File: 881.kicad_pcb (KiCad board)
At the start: 2 copper layers, 38 x 105 mm, 79 parts, among them J1 BD TRIG, J10 CY TRIG, J11 OH TRIG, J12 CH_TRIG, J13 ACCENT IN, J14 RUN/STOP, J15 RESET, J16 CLOCK OUT, J17 ACCENT OUT, J2 SD TRIG, J3 LT TRIG, J4 MT TRIG, J5 HT_TRIG, J6 RS TRIG, J7 CP_TRIG, J8 MA_TRIG, J9 CB TRIG, P1 CONN_02X03, P2 CONN_02X10, SW1 SPDT, U1 CD4048B, U2 CD4048B, X1 SYNC24 OUT, X2 MIDI OUT

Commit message: placed and routed
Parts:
- SW1: footprint MyModules:SS-12F45-1P2T-SLIDE -> MyModules:SS-12F108-1P2T-SLIDE
- moved C3 75.1 mm to (142.8, 71.0), turned to 0 degrees
- moved U2 74.9 mm to (143.5, 74.8)
- moved U1 74.7 mm to (116.8, 74.8)
- moved C2 73.7 mm to (114.8, 71.0), turned to 180 degrees
- moved R16 61.7 mm to (114.5, 149.2), turned to 90 degrees
- moved D25 59.8 mm to (120.2, 149.2), turned to 90 degrees
- moved D26 59.4 mm to (121.8, 149.2), turned to 270 degrees
- moved R20 58.0 mm to (146.5, 149.2), turned to 90 degrees
- moved D20 49.4 mm to (120.2, 138.2), turned to 90 degrees
- moved D19 48.9 mm to (121.8, 138.2), turned to 270 degrees
- moved D21 48.3 mm to (123.8, 138.2), turned to 270 degrees
- moved D24 46.3 mm to (136.2, 138.2), turned to 90 degrees
- moved R12 46.1 mm to (120.2, 134.8), turned to 90 degrees
- moved D22 45.5 mm to (125.2, 135.8), turned to 270 degrees
- moved R13 45.3 mm to (126.8, 136.0), turned to 90 degrees
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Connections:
- U1 pad 11: /RS_TRIG -> /BD_TRIG
- U1 pad 12: /CP_TRIG -> /SD_TRIG
- U1 pad 13: /SD_TRIG -> /CP_TRIG
- U1 pad 14: /BD_TRIG -> /RS_TRIG
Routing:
- net +5V: track 0.00 -> 218.0 mm, vias 0 -> 12
- net Net-(SW1-Pad2): track 0.00 -> 90.9 mm, vias 0 -> 1
- net /CY_TRIG: track 0.00 -> 87.8 mm, vias 0 -> 1
- net /OH_TRIG: track 0.00 -> 86.1 mm, vias 0 -> 1
- net GND: track 0.00 -> 76.8 mm, vias 0 -> 9
- net COMMON_TRIG: track 0.00 -> 75.4 mm, vias 0 -> 1
- net /CH_TRIG: track 0.00 -> 75.2 mm, vias 0 -> 3
- net /CP_TRIG: track 0.00 -> 69.3 mm, vias 0 -> 2
- net /CB_TRIG: track 0.00 -> 68.2 mm
- net /TRIG: track 0.00 -> 65.2 mm
- net /MA_TRIG: track 0.00 -> 59.3 mm, vias 0 -> 1
- net /MT_TRIG: track 0.00 -> 59.1 mm, vias 0 -> 2
- net /ACCENT: track 0.00 -> 58.8 mm, vias 0 -> 1
- net /RS_TRIG: track 0.00 -> 55.3 mm
- net /LT_TRIG: track 0.00 -> 47.2 mm, vias 0 -> 1
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- added copper zone on B.Cu, net GND
- added copper zone on F.Cu, net GND
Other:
- net class Default: via_dia 0.6 -> 0.8
- net class POWER added: clearance 0.25, trace_width 0.35, via_dia 0.9, via_drill 0.45

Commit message: ground stitching, tweaking
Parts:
- moved R17 0.60 mm to (121.3, 79.4)
- moved D27 0.35 mm to (121.5, 80.9)
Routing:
- net GND: track 76.8 -> 91.6 mm, vias 9 -> 13
- net Net-(D27-Pad2): track 5.50 -> 7.55 mm
- net /HT_TRIG: track 46.9 -> 48.0 mm
- net /CY_TRIG: track 87.8 -> 88.8 mm
- net +5V: track 218.0 -> 217.0 mm
- net UART_TX: track 15.4 -> 16.3 mm
- net /CH_TRIG: track 75.2 -> 76.0 mm
- net /CB_TRIG: track 68.2 -> 68.9 mm
- net /LT_TRIG: track 47.2 -> 47.9 mm
- net /MT_TRIG: track 59.1 -> 59.7 mm

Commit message: first prototype PCB ordered
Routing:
- net +5V: track 217.0 -> 217.6 mm
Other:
- rule pad_to_mask_clearance: 0.2 -> 0.025
- board text added: "881"
- board text added: "CLOCK OUT"
- board text added: "MIDI OUT"
- board text added: "RESET"
- board text added: "RUN/STOP"
- board text added: "SYNC24"
- board text added: "TRIGGER EXPANDER"
- board text added: "r1.0 10/2018"
- board text added: "system80.net"

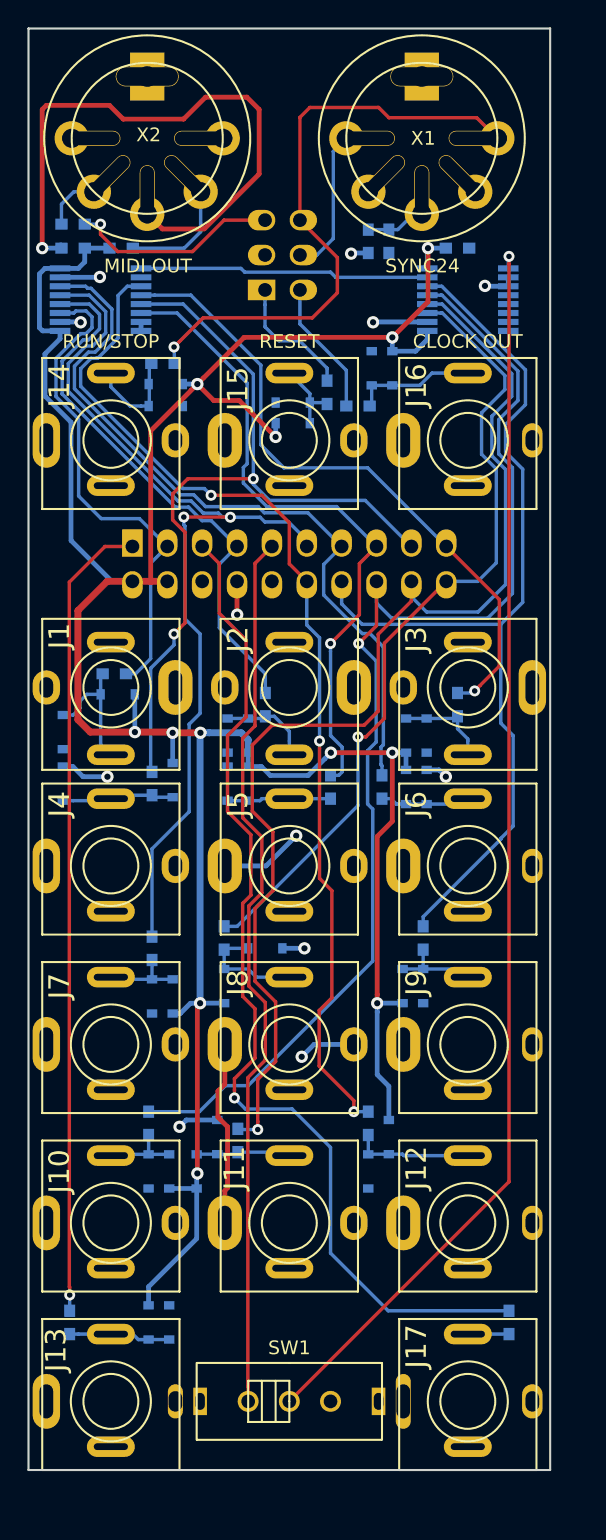
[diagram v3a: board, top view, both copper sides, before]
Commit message: schematic and footprint almost complete. spi clock or run-stop line for TII active indication still debatable, but leaning towards SPI SCK for LED indication
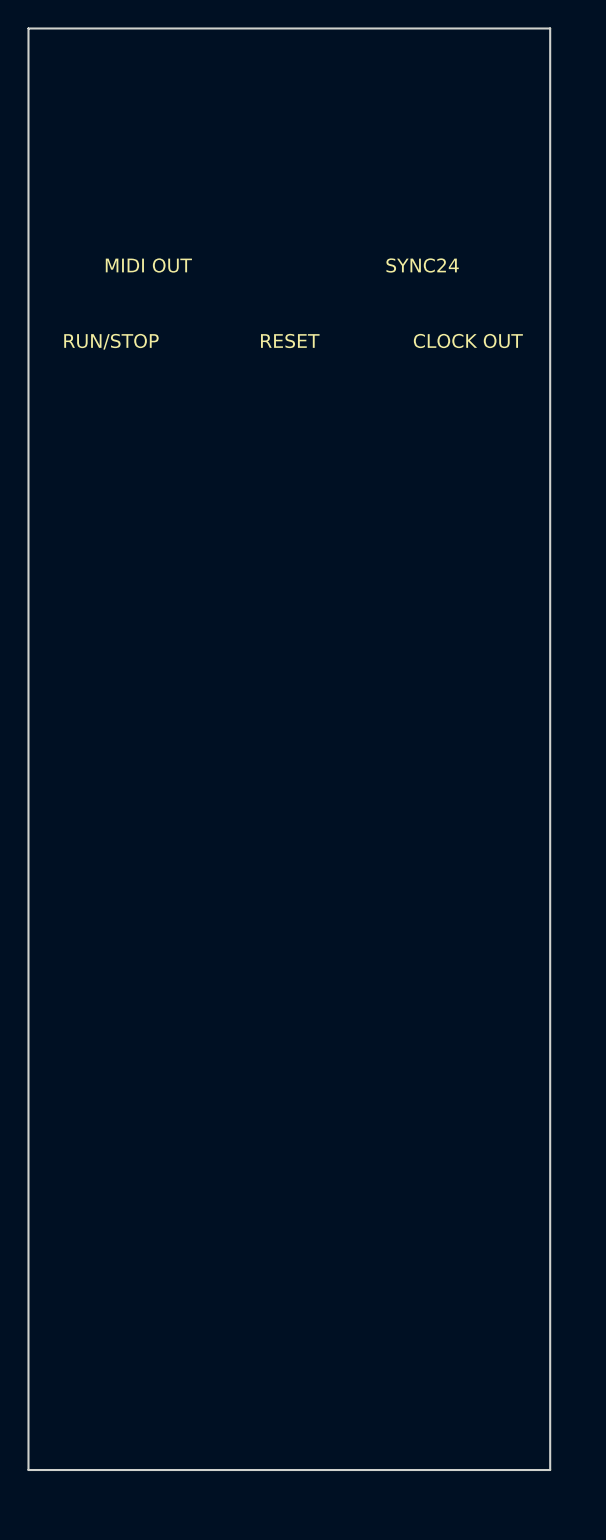
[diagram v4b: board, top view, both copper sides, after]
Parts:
- removed C1: 0.01µ, MyModules:SM0603-C-MURATA
- removed C2, C3: 0.1µ, MyModules:SM0603-C-MURATA
- removed D1, D10, D11, D12, D13, D14, D15, D16, D17, D18, D19, D2, D20, D21, D22, D23, D24, D25, D26, D27, D28, D29, D3, D30, D31, D32, D4, D5, D6, D7, D8, D9: NSR0530HT1G, MyModules:SOD323-C1A2
- removed J1: BD TRIG, MyModules:PJ-301B-JACK-SLOTS
- removed J10: CY TRIG, MyModules:PJ-301B-JACK-SLOTS
- removed J11: OH TRIG, MyModules:PJ-301B-JACK-SLOTS
- removed J12: CH_TRIG, MyModules:PJ-301B-JACK-SLOTS
- removed J13: ACCENT IN, MyModules:PJ-301B-JACK-SLOTS
- removed J14: RUN/STOP, MyModules:PJ-301B-JACK-SLOTS
- removed J15: RESET, MyModules:PJ-301B-JACK-SLOTS
- removed J16: CLOCK OUT, MyModules:PJ-301B-JACK-SLOTS
- removed J17: ACCENT OUT, MyModules:PJ-301B-JACK-SLOTS
- removed J2: SD TRIG, MyModules:PJ-301B-JACK-SLOTS
- removed J3: LT TRIG, MyModules:PJ-301B-JACK-SLOTS
- removed J4: MT TRIG, MyModules:PJ-301B-JACK-SLOTS
- removed J5: HT_TRIG, MyModules:PJ-301B-JACK-SLOTS
- removed J6: RS TRIG, MyModules:PJ-301B-JACK-SLOTS
- removed J7: CP_TRIG, MyModules:PJ-301B-JACK-SLOTS
- removed J8: MA_TRIG, MyModules:PJ-301B-JACK-SLOTS
- removed J9: CB TRIG, MyModules:PJ-301B-JACK-SLOTS
- removed P1: CONN_02X03, w_conn_strip:vasch_strip_3x2
- removed P2: CONN_02X10, w_conn_strip:vasch_strip_10x2
- removed R1, R10, R11, R12, R13, R14, R15, R16, R17, R18, R19, R2, R20, R3, R4, R6, R7, R8, R9: 220, MyModules:SM0603-R-YAGEO
- removed R5: 22, MyModules:SM0603-R-YAGEO
- removed SW1: SPDT, MyModules:SS-12F108-1P2T-SLIDE
- removed U1, U2: CD4048B, Housings_SSOP:TSSOP-16_4.4x5mm_Pitch0.65mm
- removed X1: SYNC24 OUT, MyModules:SD-50BV-5DIN-SLOTS
- removed X2: MIDI OUT, MyModules:SD-50BV-5DIN-SLOTS
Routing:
- net +5V: track 217.6 -> 0.00 mm, vias 12 -> 0
- net GND: track 91.6 -> 0.00 mm, vias 13 -> 0
- net Net-(SW1-Pad2): track 90.9 -> 0.00 mm, vias 1 -> 0
- net /CY_TRIG: track 88.8 -> 0.00 mm, vias 1 -> 0
- net /OH_TRIG: track 86.3 -> 0.00 mm, vias 1 -> 0
- net /CH_TRIG: track 76.0 -> 0.00 mm, vias 3 -> 0
- net COMMON_TRIG: track 75.4 -> 0.00 mm, vias 1 -> 0
- net /CP_TRIG: track 69.3 -> 0.00 mm, vias 2 -> 0
- net /CB_TRIG: track 68.9 -> 0.00 mm
- net /TRIG: track 65.2 -> 0.00 mm
- net /MT_TRIG: track 59.8 -> 0.00 mm, vias 2 -> 0
- net /MA_TRIG: track 59.3 -> 0.00 mm, vias 1 -> 0
- net /ACCENT: track 58.8 -> 0.00 mm, vias 1 -> 0
- net /RS_TRIG: track 55.3 -> 0.00 mm
- net /HT_TRIG: track 48.0 -> 0.00 mm, vias 1 -> 0
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- removed copper zone on B.Cu, net GND
- removed copper zone on F.Cu, net GND
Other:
- board text added: "r2.0 10/2020"
- board text removed: "881"
- board text removed: "r1.0 10/2018"

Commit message: first route
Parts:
- added C1: 0.01µ, MyModules:SM0603-C-MURATA, B.Cu at (121.5, 91.8)
- added C15: 1µ, Capacitors_SMD:C_0805, B.Cu at (129.5, 79.0)
- added C19: 0.1µ, MyModules:SM0603-C-MURATA, B.Cu at (129.2, 77.2)
- added C2: 0.1µ, MyModules:SM0603-C-MURATA, B.Cu at (115.0, 76.5)
- added C20: 0.1µ, MyModules:SM0603-C-MURATA, B.Cu at (143.5, 76.8)
- added C3: 0.1µ, MyModules:SM0603-C-MURATA, B.Cu at (137.0, 76.5)
- added C4: 1n, MyModules:SM0603-C-MURATA, B.Cu at (134.2, 152.2)
- added D1: B5819W, Diodes_SMD:D_SOD-123, B.Cu at (115.8, 153.5)
- added D10: 1N4148, Diodes_SMD:D_SOD-323F, B.Cu at (141.8, 114.0)
- added D11: 1N4148, Diodes_SMD:D_SOD-323F, B.Cu at (115.8, 127.0)
- added D12: 1N4148, Diodes_SMD:D_SOD-323F, B.Cu at (128.8, 127.0)
- added D13: 1N4148, Diodes_SMD:D_SOD-323F, B.Cu at (141.8, 127.0)
- added D14: 1N4148, Diodes_SMD:D_SOD-323F, B.Cu at (115.8, 140.0)
- added D15: 1N4148, Diodes_SMD:D_SOD-323F, B.Cu at (128.8, 140.0)
- added D16: 1N4148, Diodes_SMD:D_SOD-323F, B.Cu at (141.8, 139.8)
- added D17: LED, LEDs:LED_0805, B.Cu at (130.5, 155.0)
- added D18: LED, LEDs:LED_D3.0mm, F.Cu at (130.5, 153.8)
- added D2: B5819W, Diodes_SMD:D_SOD-123, B.Cu at (119.5, 153.5)
- added D3: B5819W, Diodes_SMD:D_SOD-123, B.Cu at (141.8, 153.8)
- added D4: B5819W, Diodes_SMD:D_SOD-123, B.Cu at (145.5, 153.8)
- added D5: 1N4148, Diodes_SMD:D_SOD-323F, B.Cu at (116.0, 101.0)
- added D6: 1N4148, Diodes_SMD:D_SOD-323F, B.Cu at (129.0, 101.0)
- added D7: 1N4148, Diodes_SMD:D_SOD-323F, B.Cu at (141.9, 101.0)
- added D8: 1N4148, Diodes_SMD:D_SOD-323F, B.Cu at (115.8, 114.0)
- added D9: 1N4148, Diodes_SMD:D_SOD-323F, B.Cu at (128.8, 114.0)
- added ISP1: CONN_02X03, w_conn_strip:vasch_strip_3x2, B.Cu at (130.5, 88.5)
- added J1: RUN/STOP, MyModules:PJ-301B-JACK-SLOTS, F.Cu at (120.0, 61.0)
- added J10: RS IN, MyModules:PJ-301B-JACK-SLOTS, F.Cu at (143.5, 116.0)
- added J11: CP IN, MyModules:PJ-301B-JACK-SLOTS, F.Cu at (117.5, 129.0)
- added J12: MA IN, MyModules:PJ-301B-JACK-SLOTS, F.Cu at (130.5, 129.0)
- added J13: CB IN, MyModules:PJ-301B-JACK-SLOTS, F.Cu at (143.5, 129.0)
- added J14: CY IN, MyModules:PJ-301B-JACK-SLOTS, F.Cu at (117.5, 142.0)
- added J15: OH IN, MyModules:PJ-301B-JACK-SLOTS, F.Cu at (130.5, 142.0)
- added J16: CH IN, MyModules:PJ-301B-JACK-SLOTS, F.Cu at (143.5, 142.0)
- added J2: SYNC24 CLK, MyModules:PJ-301B-JACK-SLOTS, F.Cu at (141.0, 61.0)
- added J3: ASSIGN 1, MyModules:PJ-301B-JACK-SLOTS, F.Cu at (117.5, 155.0)
- added J4: ASSIGN 2, MyModules:PJ-301B-JACK-SLOTS, F.Cu at (143.5, 155.0)
- added J5: BD IN, MyModules:PJ-301B-JACK-SLOTS, F.Cu at (117.5, 103.0)
- added J6: SD IN, MyModules:PJ-301B-JACK-SLOTS, F.Cu at (130.5, 103.0)
- added J7: LT IN, MyModules:PJ-301B-JACK-SLOTS, F.Cu at (143.5, 103.0)
- added J8: MT IN, MyModules:PJ-301B-JACK-SLOTS, F.Cu at (117.5, 116.0)
- added J9: HT IN, MyModules:PJ-301B-JACK-SLOTS, F.Cu at (130.5, 116.0)
- added P1: CONN_02X03, w_conn_strip:vasch_strip_4x2, B.Cu at (130.5, 64.5)
- added Q1: MMBT3904, MyModules:SOT23-132-JRL, B.Cu at (121.2, 98.8)
- added Q10: MMBT3904, MyModules:SOT23-132-JRL, B.Cu at (121.2, 137.8)
- added Q11: MMBT3904, MyModules:SOT23-132-JRL, B.Cu at (134.2, 137.8)
- added Q12: MMBT3904, MyModules:SOT23-132-JRL, B.Cu at (147.2, 137.8)
- added Q13: MMBT3904, MyModules:SOT23-132-JRL, B.Cu at (135.0, 147.8)
- added Q14: MMBT3906, SOT-23, B.Cu at (130.5, 150.5)
- added Q2: MMBT3904, MyModules:SOT23-132-JRL, B.Cu at (134.2, 98.8)
- added Q3: MMBT3904, MyModules:SOT23-132-JRL, B.Cu at (147.5, 98.8)
- added Q4: MMBT3904, MyModules:SOT23-132-JRL, B.Cu at (121.2, 111.8)
- added Q5: MMBT3904, MyModules:SOT23-132-JRL, B.Cu at (134.2, 111.8)
- added Q6: MMBT3904, MyModules:SOT23-132-JRL, B.Cu at (147.2, 111.8)
- added Q7: MMBT3904, MyModules:SOT23-132-JRL, B.Cu at (121.2, 124.8)
- added Q8: MMBT3904, MyModules:SOT23-132-JRL, B.Cu at (134.2, 124.8)
- added Q9: MMBT3904, MyModules:SOT23-132-JRL, B.Cu at (147.2, 124.8)
- added R1: 220, MyModules:SM0603-R-YAGEO, B.Cu at (138.2, 83.0)
- added R10: 100K, MyModules:SM0603-R-YAGEO, B.Cu at (119.0, 101.0)
- added R11: 100K, MyModules:SM0603-R-YAGEO, B.Cu at (132.0, 101.0)
- added R12: 100K, MyModules:SM0603-R-YAGEO, B.Cu at (145.2, 101.0)
- added R13: 100K, MyModules:SM0603-R-YAGEO, B.Cu at (119.0, 114.0)
- added R14: 10K, MyModules:SM0603-R-YAGEO, B.Cu at (120.2, 96.0)
- added R15: 10K, MyModules:SM0603-R-YAGEO, B.Cu at (136.2, 96.2)
- added R16: 10K, MyModules:SM0603-R-YAGEO, B.Cu at (146.5, 96.0)
- added R17: 10K, MyModules:SM0603-R-YAGEO, B.Cu at (120.2, 109.0)
- added R18: 100K, MyModules:SM0603-R-YAGEO, B.Cu at (130.5, 114.0)
- added R19: 100K, MyModules:SM0603-R-YAGEO, B.Cu at (143.5, 114.0)
- added R2: 22, MyModules:SM0603-R-YAGEO, B.Cu at (120.0, 91.8)
- added R20: 100K, MyModules:SM0603-R-YAGEO, B.Cu at (117.5, 127.0)
- added R21: 100K, MyModules:SM0603-R-YAGEO, B.Cu at (130.5, 127.0)
- added R22: 100K, MyModules:SM0603-R-YAGEO, B.Cu at (132.0, 114.0)
- added R23: 100K, MyModules:SM0603-R-YAGEO, B.Cu at (145.0, 114.0)
- added R24: 100K, MyModules:SM0603-R-YAGEO, B.Cu at (119.0, 127.0)
- added R25: 100K, MyModules:SM0603-R-YAGEO, B.Cu at (132.0, 127.0)
- added R26: 10K, MyModules:SM0603-R-YAGEO, B.Cu at (133.2, 109.0)
- added R27: 10K, MyModules:SM0603-R-YAGEO, B.Cu at (146.2, 109.0)
- added R28: 10K, MyModules:SM0603-R-YAGEO, B.Cu at (120.2, 122.0)
- added R29: 10K, MyModules:SM0603-R-YAGEO, B.Cu at (133.2, 122.0)
- added R3: 220, MyModules:SM0603-R-YAGEO, B.Cu at (143.8, 83.0)
- added R30: 100K, MyModules:SM0603-R-YAGEO, B.Cu at (143.5, 127.0)
- added R31: 100K, MyModules:SM0603-R-YAGEO, B.Cu at (117.5, 140.0)
- added R32: 100K, MyModules:SM0603-R-YAGEO, B.Cu at (130.5, 140.0)
- added R33: 100K, MyModules:SM0603-R-YAGEO, B.Cu at (143.5, 140.0)
- added R34: 100K, MyModules:SM0603-R-YAGEO, B.Cu at (145.0, 127.0)
- added R35: 100K, MyModules:SM0603-R-YAGEO, B.Cu at (119.0, 140.0)
- added R36: 100K, MyModules:SM0603-R-YAGEO, B.Cu at (132.0, 140.0)
- added R37: 100K, MyModules:SM0603-R-YAGEO, B.Cu at (145.0, 140.0)
- added R38: 10K, MyModules:SM0603-R-YAGEO, B.Cu at (146.2, 122.0)
- added R39: 10K, MyModules:SM0603-R-YAGEO, B.Cu at (120.2, 135.0)
- added R4: 1K, MyModules:SM0603-R-YAGEO, B.Cu at (121.2, 149.5)
- added R40: 10K, MyModules:SM0603-R-YAGEO, B.Cu at (133.2, 135.0)
- added R41: 10K, MyModules:SM0603-R-YAGEO, B.Cu at (146.0, 135.0)
- added R42: 47K, MyModules:SM0603-R-YAGEO, B.Cu at (122.2, 151.8)
- added R43: 100K, MyModules:SM0603-R-YAGEO, B.Cu at (148.2, 151.8)
- added R44: 47K, MyModules:SM0603-R-YAGEO, B.Cu at (147.0, 80.0)
- added R45: 47K, MyModules:SM0603-R-YAGEO, B.Cu at (148.5, 80.0)
- added R46: 100K, MyModules:SM0603-R-YAGEO, B.Cu at (135.0, 145.0)
- added R47: 1K, MyModules:SM0603-R-YAGEO, B.Cu at (137.0, 150.2)
- added R48: 10K, MyModules:SM0603-R-YAGEO, B.Cu at (134.2, 150.8)
- added R49: 1K, MyModules:SM0603-R-YAGEO, B.Cu at (134.5, 155.0)
- added R5: 1K, MyModules:SM0603-R-YAGEO, B.Cu at (147.2, 149.5)
- added R6: 100K, MyModules:SM0603-R-YAGEO, B.Cu at (117.5, 101.0)
- added R7: 100K, MyModules:SM0603-R-YAGEO, B.Cu at (130.5, 101.0)
- added R8: 100K, MyModules:SM0603-R-YAGEO, B.Cu at (143.8, 101.0)
- added R9: 100K, MyModules:SM0603-R-YAGEO, B.Cu at (117.5, 114.0)
- added TP2: CONN_1, MyModules:TEST_POINT_LOOP_4592, B.Cu at (126.5, 56.5)
- added U1: 74HC165, Housings_SOIC:SOIC-16_3.9x9.9mm_Pitch1.27mm, B.Cu at (119.5, 71.0)
- added U2: 74HC165, Housings_SOIC:SOIC-16_3.9x9.9mm_Pitch1.27mm, B.Cu at (141.5, 71.0)
- added U7: 74AHCT1G125GW, TO_SOT_Packages_SMD:SOT-353_SC-70-5, B.Cu at (146.2, 76.8)
- added X1: MIDI OUT, MyModules:SD-50BV-5DIN, F.Cu at (141.0, 83.0)
- added X2: SYNC24, MyModules:SD-50BV-5DIN, F.Cu at (120.0, 83.0)
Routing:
- net DIN_RESET: track 0.00 -> 143.3 mm, vias 0 -> 1
- net ISP_SCK: track 0.00 -> 117.2 mm, vias 0 -> 3
- net DIN_FILL: track 0.00 -> 109.5 mm, vias 0 -> 1
- net /HT: track 0.00 -> 85.3 mm
- net /CY: track 0.00 -> 77.1 mm, vias 0 -> 2
- net /RS: track 0.00 -> 75.7 mm, vias 0 -> 2
- net /CH: track 0.00 -> 72.6 mm, vias 0 -> 2
- net /OH: track 0.00 -> 67.1 mm, vias 0 -> 2
- net DIN_RUN_STOP: track 0.00 -> 67.0 mm, vias 0 -> 1
- net /MA: track 0.00 -> 60.5 mm, vias 0 -> 2
- net /CP: track 0.00 -> 56.4 mm, vias 0 -> 2
- net /CB: track 0.00 -> 54.5 mm, vias 0 -> 2
- net DIN_TEMPO_CLK: track 0.00 -> 53.4 mm
- net /LT: track 0.00 -> 52.5 mm
- net ISP_MOSI: track 0.00 -> 47.2 mm, vias 0 -> 2
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- added copper zone on In2.Cu, net +5V
- added copper zone on B.Cu, net GNDD
- added copper zone on F.Cu, net GNDD
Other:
- copper layers 2 -> 4
- net class Default: via_dia 0.8 -> 0.9; via_drill 0.4 -> 0.45
- net class POWER: via_dia 0.9 -> 1; via_drill 0.45 -> 0.5

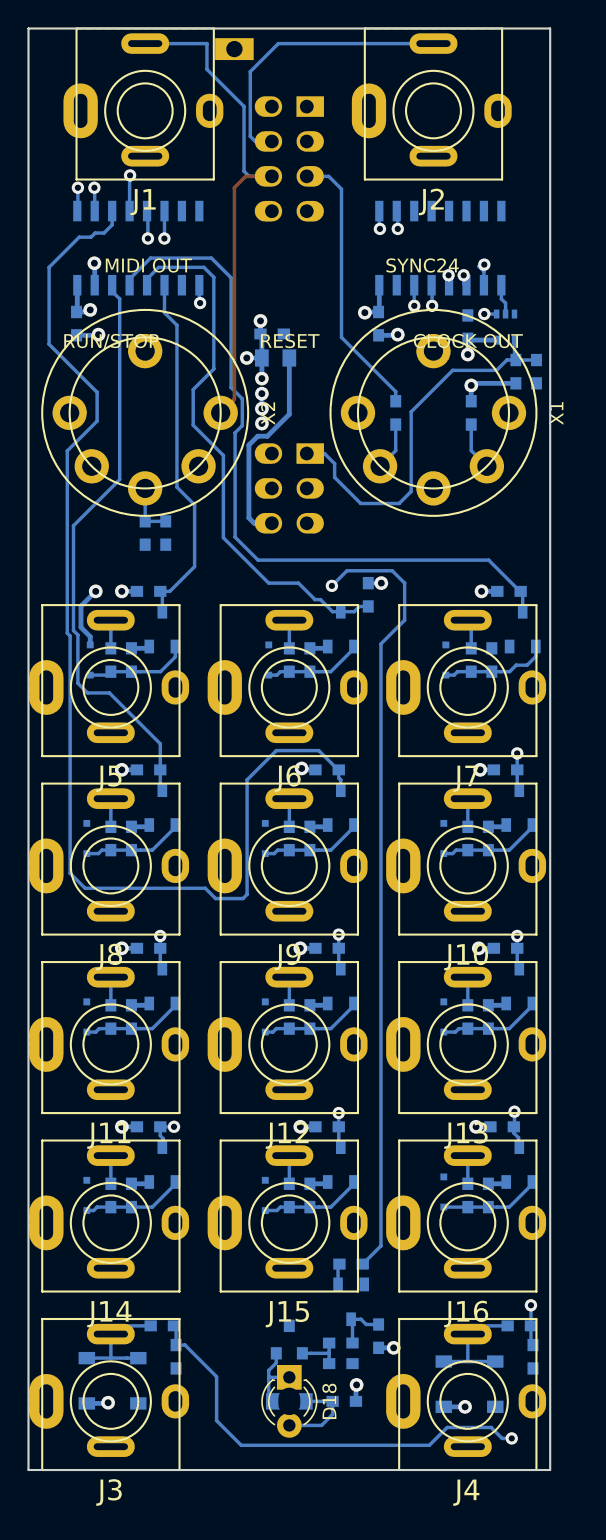
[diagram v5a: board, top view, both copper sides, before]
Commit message: routed with more finesse
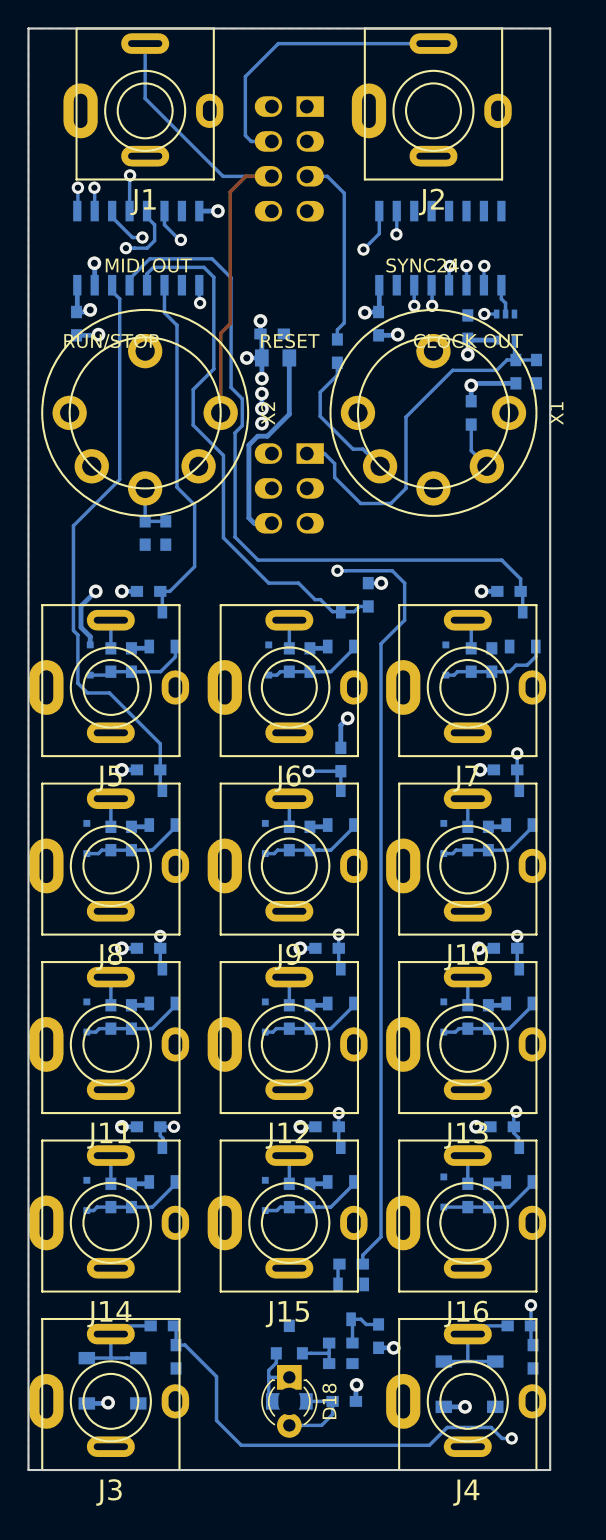
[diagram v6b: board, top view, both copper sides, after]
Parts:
- removed TP2: CONN_1, MyModules:TEST_POINT_LOOP_4592
- moved R1 6.19 mm to (134.0, 78.5)
- moved R26 1.25 mm to (134.2, 108.2), turned to 270 degrees
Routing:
- net /HT: track 85.3 -> 52.0 mm, vias 0 -> 2
- net Net-(R1-Pad1): track 3.51 -> 10.3 mm
- net UART_TX: track 20.0 -> 14.1 mm
- net ISP_SCK: track 117.2 -> 112.5 mm
- net /CP: track 56.4 -> 58.6 mm
- net /CY: track 77.1 -> 79.2 mm
- net DIN_RESET: track 143.3 -> 144.9 mm
- net DIN_RUN_STOP: track 67.0 -> 65.5 mm
- net GNDD: track 39.3 -> 40.6 mm, vias 4 -> 5
- net +5V: track 40.7 -> 42.0 mm
- net ISP_MOSI: track 47.2 -> 48.4 mm
- net /CB: track 54.5 -> 55.6 mm
- net DIN_FILL: track 109.5 -> 110.4 mm
- net /MA: track 60.5 -> 61.2 mm

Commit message: routed, finessed, ready to order me thinks
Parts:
- removed R45: 47K, MyModules:SM0603-R-YAGEO
- added SNAP-HOLE-0.125-INCH: VAL**, MyModules:SNAP_HOLE_0.125_INCH, F.Cu at (143.3, 93.9)
- added SNAP-HOLE-0.125-INCH: VAL**, MyModules:SNAP_HOLE_0.125_INCH, F.Cu at (124.0, 147.9)
- added SNAP-HOLE-0.125-INCH: VAL**, MyModules:SNAP_HOLE_0.125_INCH, F.Cu at (131.7, 75.8)
- added SNAP-HOLE-0.125-INCH: VAL**, MyModules:SNAP_HOLE_0.125_INCH, F.Cu at (114.5, 93.8)
- moved R4 3.09 mm to (118.5, 148.1)
- moved C19 1.25 mm to (128.5, 76.2), turned to 90 degrees
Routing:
- net DIN_RESET: track 144.9 -> 150.6 mm
- net DIN_FILL: track 110.4 -> 113.9 mm
- net +5V: track 42.0 -> 44.9 mm, vias 26 -> 28
- net /LT: track 53.0 -> 54.8 mm
- net ISP_MISO: track 27.7 -> 26.2 mm
- net /RS: track 75.7 -> 74.9 mm
- net ISP_SCK: track 112.5 -> 111.7 mm
- net DIN_TEMPO_CLK: track 53.9 -> 53.2 mm
- net DIN_RUN_STOP: track 65.5 -> 65.0 mm
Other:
- board text added: "881"
- board text added: "AC/1"
- board text added: "BD"
- board text added: "CB"
- board text added: "CH"
- board text added: "CP"
- board text added: "CY"
- board text added: "DIN EXP"
- board text added: "HT/HC"
- board text added: "LT/LC"
- board text added: "MA"
- board text added: "MT/MC"
- board text added: "OH"
- board text added: "RS/CL"
- board text added: "SD"
- board text added: "SEL/2"
- board text removed: "RESET"
- board text removed: "TRIGGER EXPANDER"
